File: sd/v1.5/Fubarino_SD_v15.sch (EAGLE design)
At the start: 37 parts, among them IC1 PIC32MX440F256H-80I/PT, IC2 MCP1702T-3302E/MB, J1 MICRO_SD_CARD_SOCKET, J2 M28USEPIN1, J3 M28NOPIN1, J8 USB-5PIN, Q1 8MHz, Q2 32.768 KHz

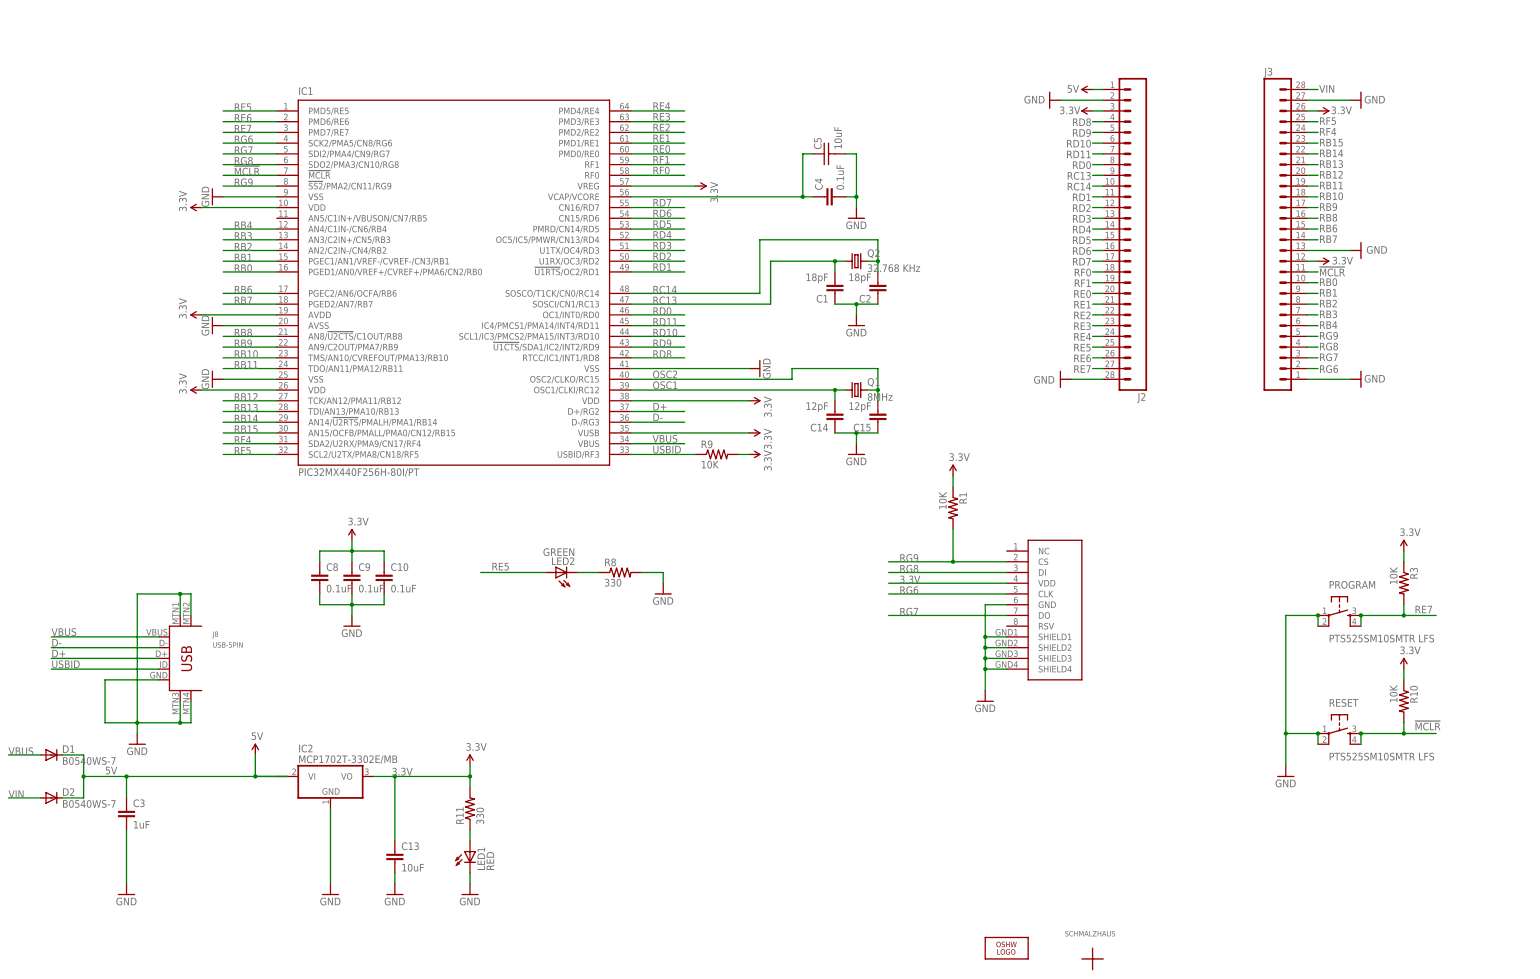
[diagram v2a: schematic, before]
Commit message: Created PIC32MX795F512H symbol, and updated schematic with it. Also had to re-do nets to CPU on layout because Eagle reasons.
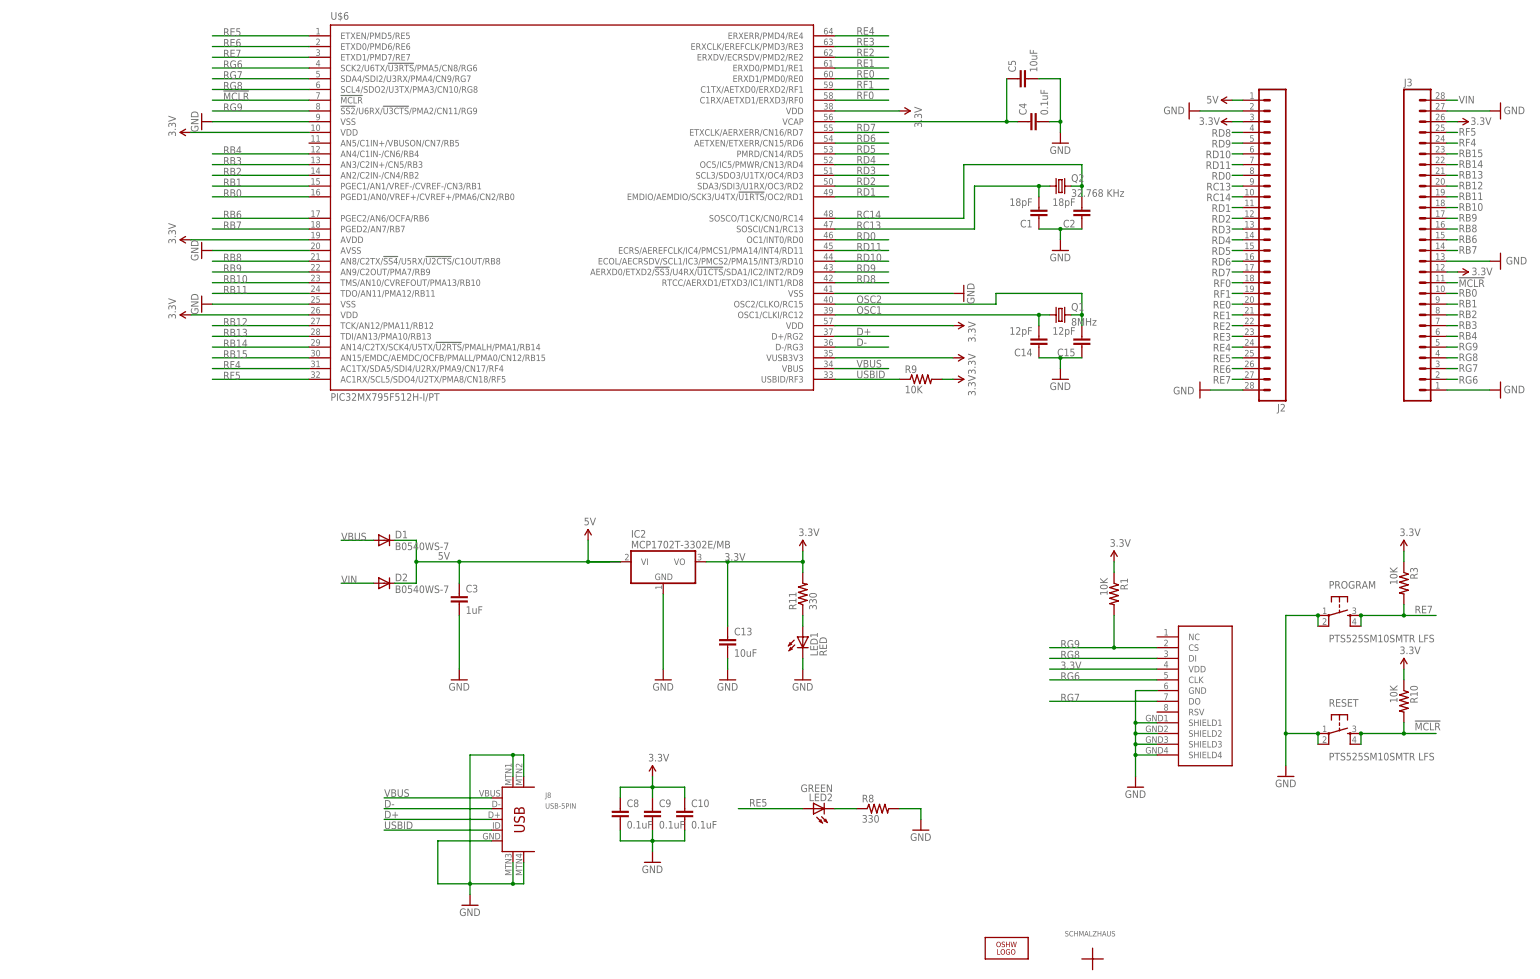
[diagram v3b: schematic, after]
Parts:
- removed IC1: PIC32MX440F256H-80I/PT, SchmalzHaus:PIC32MX440F256H
- added U$6: PIC32MX795F512H-I/PT, SchmalzHaus:PIC32MX795F512H-I/PT
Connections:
- net !MCLR!: now also U$6.!MCLR; no longer IC1.!MCLR
- net 3.3V: now also U$6.AVDD, U$6.VDD, U$6.VDD@2, U$6.VDD@3, U$6.VDD@5, U$6.VUSB3V3; no longer IC1.AVDD, IC1.VDD@2, IC1.VDD@3, IC1.VDD@5, IC1.VREG, IC1.VUSB
- net D+: now also U$6.D+/RG2; no longer IC1.D+/RG2
- net D-: now also U$6.D-/RG3; no longer IC1.D-/RG3
- net GND: now also U$6.AVSS, U$6.VSS@2, U$6.VSS@3, U$6.VSS@5; no longer IC1.AVSS, IC1.VSS@2, IC1.VSS@3, IC1.VSS@5
- net N$110: now also U$6.VCAP; no longer IC1.VCAP/VCORE
- net OSC1: now also U$6.OSC1/CLKI/RC12; no longer IC1.OSC1/CLKI/RC12
- net OSC2: now also U$6.OSC2/CLKO/RC15; no longer IC1.OSC2/CLKO/RC15
- net RB0: now also U$6.PGED1/AN0/VREF+/CVREF+/PMA6/CN2/RB0; no longer IC1.PGED1/AN0/VREF+/CVREF+/PMA6/CN2/RB0
- net RB1: now also U$6.PGEC1/AN1/VREF-/CVREF-/CN3/RB1; no longer IC1.PGEC1/AN1/VREF-/CVREF-/CN3/RB1
- net RB10: now also U$6.TMS/AN10/CVREFOUT/PMA13/RB10; no longer IC1.TMS/AN10/CVREFOUT/PMA13/RB10
- net RB11: now also U$6.TDO/AN11/PMA12/RB11; no longer IC1.TDO/AN11/PMA12/RB11
- net RB12: now also U$6.TCK/AN12/PMA11/RB12; no longer IC1.TCK/AN12/PMA11/RB12
- net RB13: now also U$6.TDI/AN13/PMA10/RB13; no longer IC1.TDI/AN13/PMA10/RB13
- net RB14: now also U$6.AN14/C2TX/SCK4/U5TX/!U2RTS!/PMALH/PMA1/RB14; no longer IC1.AN14/!U2RTS!/PMALH/PMA1/RB14
- net RB15: now also U$6.AN15/EMDC/AEMDC/OCFB/PMALL/PMA0/CN12/RB15; no longer IC1.AN15/OCFB/PMALL/PMA0/CN12/RB15
- net RB2: now also U$6.AN2/C2IN-/CN4/RB2; no longer IC1.AN2/C2IN-/CN4/RB2
- net RB3: now also U$6.AN3/C2IN+/CN5/RB3; no longer IC1.AN3/C2IN+/CN5/RB3
- net RB4: now also U$6.AN4/C1IN-/CN6/RB4; no longer IC1.AN4/C1IN-/CN6/RB4
- net RB6: now also U$6.PGEC2/AN6/OCFA/RB6; no longer IC1.PGEC2/AN6/OCFA/RB6
- net RB7: now also U$6.PGED2/AN7/RB7; no longer IC1.PGED2/AN7/RB7
- net RB8: now also U$6.AN8/C2TX/!SS4!/U5RX/!U2CTS!/C1OUT/RB8; no longer IC1.AN8/!U2CTS!/C1OUT/RB8
- net RB9: now also U$6.AN9/C2OUT/PMA7/RB9; no longer IC1.AN9/C2OUT/PMA7/RB9
- net RC13: now also U$6.SOSCI/CN1/RC13; no longer IC1.SOSCI/CN1/RC13
- net RC14: now also U$6.SOSCO/T1CK/CN0/RC14; no longer IC1.SOSCO/T1CK/CN0/RC14
- net RD0: now also U$6.OC1/INT0/RD0; no longer IC1.OC1/INT0/RD0
- net RD1: now also U$6.EMDIO/AEMDIO/SCK3/U4TX/!U1RTS!/OC2/RD1; no longer IC1.!U1RTS!/OC2/RD1
- net RD10: now also U$6.ECOL/AECRSDV/SCL1/IC3/PMCS2/PMA15/INT3/RD10; no longer IC1.SCL1/IC3/PMCS2/PMA15/INT3/RD10
- net RD11: now also U$6.ECRS/AEREFCLK/IC4/PMCS1/PMA14/INT4/RD11; no longer IC1.IC4/PMCS1/PMA14/INT4/RD11
- net RD2: now also U$6.SDA3/SDI3/U1RX/OC3/RD2; no longer IC1.U1RX/OC3/RD2
- net RD3: now also U$6.SCL3/SDO3/U1TX/OC4/RD3; no longer IC1.U1TX/OC4/RD3
- net RD4: now also U$6.OC5/IC5/PMWR/CN13/RD4; no longer IC1.OC5/IC5/PMWR/CN13/RD4
- net RD5: now also U$6.PMRD/CN14/RD5; no longer IC1.PMRD/CN14/RD5
- net RD6: now also U$6.AETXEN/ETXERR/CN15/RD6; no longer IC1.CN15/RD6
- net RD7: now also U$6.ETXCLK/AERXERR/CN16/RD7; no longer IC1.CN16/RD7
- net RD8: now also U$6.RTCC/AERXD1/ETXD3/IC1/INT1/RD8; no longer IC1.RTCC/IC1/INT1/RD8
- net RD9: now also U$6.AERXD0/ETXD2/!SS3!/U4RX/!U1CTS!/SDA1/IC2/INT2/RD9; no longer IC1.!U1CTS!/SDA1/IC2/INT2/RD9
- net RE0: now also U$6.ERXD1/PMD0/RE0; no longer IC1.PMD0/RE0
- net RE1: now also U$6.ERXD0/PMD1/RE1; no longer IC1.PMD1/RE1
- net RE2: now also U$6.ERXDV/ECRSDV/PMD2/RE2; no longer IC1.PMD2/RE2
- net RE3: now also U$6.ERXCLK/EREFCLK/PMD3/RE3; no longer IC1.PMD3/RE3
- net RE4: now also U$6.ERXERR/PMD4/RE4; no longer IC1.PMD4/RE4
- net RE5: now also U$6.ETXEN/PMD5/RE5; no longer IC1.PMD5/RE5
- net RE6: now also U$6.ETXD0/PMD6/RE6; no longer IC1.PMD6/RE6
- net RE7: now also U$6.ETXD1/PMD7/RE7; no longer IC1.PMD7/RE7
- net RF0: now also U$6.C1RX/AETXD1/ERXD3/RF0; no longer IC1.RF0
- net RF1: now also U$6.C1TX/AETXD0/ERXD2/RF1; no longer IC1.RF1
- net RF4: now also U$6.AC1TX/SDA5/SDI4/U2RX/PMA9/CN17/RF4; no longer IC1.SDA2/U2RX/PMA9/CN17/RF4
- net RF5: now also U$6.AC1RX/SCL5/SDO4/U2TX/PMA8/CN18/RF5; no longer IC1.SCL2/U2TX/PMA8/CN18/RF5
- net RG6: now also U$6.SCK2/U6TX/!U3RTS!/PMA5/CN8/RG6; no longer IC1.SCK2/PMA5/CN8/RG6
- net RG7: now also U$6.SDA4/SDI2/U3RX/PMA4/CN9/RG7; no longer IC1.SDI2/PMA4/CN9/RG7
- net RG8: now also U$6.SCL4/SDO2/U3TX/PMA3/CN10/RG8; no longer IC1.SDO2/PMA3/CN10/RG8
- net RG9: now also U$6.!SS2!/U6RX/!U3CTS!/PMA2/CN11/RG9; no longer IC1.!SS2!/PMA2/CN11/RG9
- net USBID: now also U$6.USBID/RF3; no longer IC1.USBID/RF3
- net VBUS: now also U$6.VBUS; no longer IC1.VBUS
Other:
- note added: "3/10/2014 - v1.5 (Microchip version)"
- note added: "<- Pin 1 = MCLR"
- note added: "PIC32MX440F256H-80I/PT (alt)"
- note added: "Updated CPU to MX795 symbol"
- note removed: "<- Pin 1"
- note removed: "PIC32MX795F512H-80I/PT (alt)"
- moved on the sheet: C1, C10, C13, C14, C15, C2, C3, C4, C8, C9, D1, D2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
